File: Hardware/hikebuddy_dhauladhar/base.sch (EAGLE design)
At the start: 115 parts, among them J1 4P-SMD-2.0-90D, J2 4P-2.0-90D, U11 MF-DSC-SOT233-BSS84, U3 MF-DSC-SOT233-MMBT3904, U4 MF-DSC-SOT233-MMBT3904, U9 MF-DSC-SOT233-BSS84

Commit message: added 3D models for most PCB parts
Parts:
- C16, C21, C26: device SparkFun-Capacitors:4.7UF0603 -> SparkFun-Capacitors:4.7UF-0603-6.3V-(10%)
- C2: value 2.7pF -> 4.7pF
- C24, C8: value 4.7uF -> 10uF
- C28, C29, C7, C9: value 4.7uF -> 2.2uF
- C3: value 0.22uF -> 0.1uF
- FT231: value FT231XS-U -> FT231XS-UTSSOP20; device FT231XS-U:FT231XS-U -> FT231XS-U:FT231XS-UTSSOP20; SPICEPREFIX (none) -> F
- L1: value 1.6nH -> 30Ω/1.8A
- MCP73831: value MCP73831 -> MCP73831T-3ACI/OT; device SparkFun-IC-Power:MCP73831 -> MCP73831T-3ACI_OT:MCP73831T-3ACI/OT
- PCA9555D: value PCA9555D -> PCA9555; device PCA9555:PCA9555D -> PCA9555:PCA9555
- R12, R13, R14, R31, R43: value 50k -> 10k
- R15, R29: value 27 -> 22
- R16: value 50k -> 330k
- R24: value 150k -> 47k
- R27, R28: value 150k -> 200k
- R48: value 10k -> 1k
- renumbered USB to J3
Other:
- moved on the sheet: C10, R44, R7

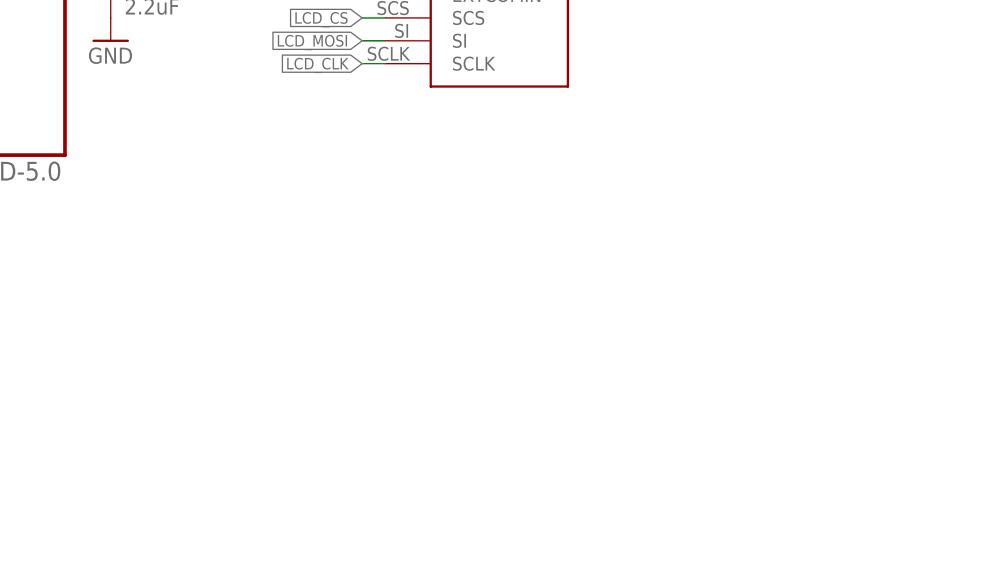
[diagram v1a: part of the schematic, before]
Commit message: added lvgl submodule
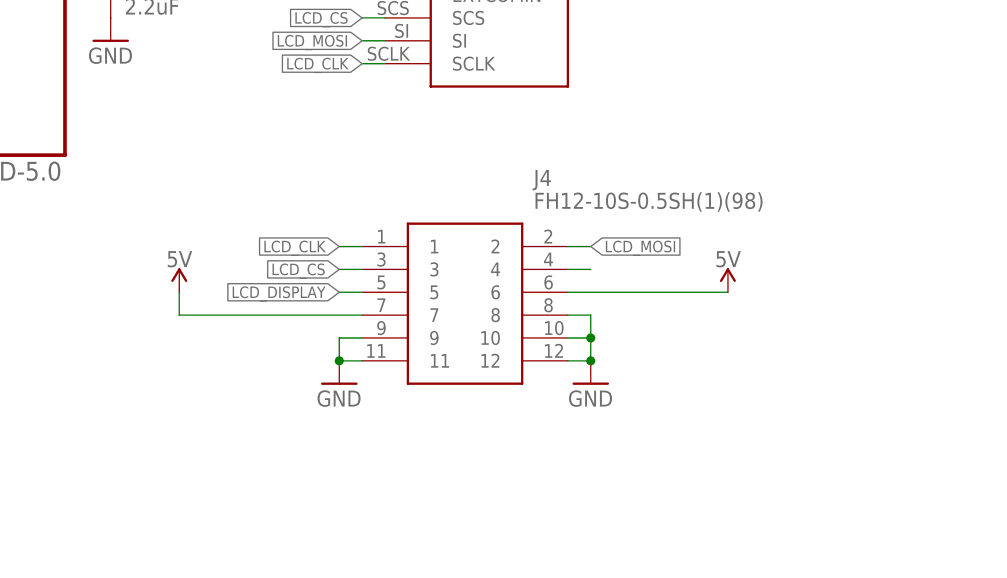
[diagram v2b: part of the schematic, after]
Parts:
- added J4: FH12-10S-0.5SH(1)(98), FH12-10S-0.5SH(1)(98):FH12-10S-0.5SH(1)(98)
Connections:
- new net N$40: J4.4
- net 5V: now also J4.6, J4.7
- net GND: now also J4.10, J4.11, J4.12, J4.8, J4.9
- net LCD_CLK: now also J4.1
- net LCD_CS: now also J4.3
- net LCD_DISPLAY: now also J4.5
- net LCD_MOSI: now also J4.2
